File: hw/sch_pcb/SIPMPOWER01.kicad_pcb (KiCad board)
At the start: 2 copper layers, 60.5 x 40.1 mm, 37 parts, among them J1 HEADER_2x01_PARALLEL, J2 HEADER_2x01_PARALLEL, J3 HEADER_2x01_PARALLEL, J4 HEADER_2x01_PARALLEL, J5 HEADER_2x01_PARALLEL, J6 JUMP2_2x1, J7 HEADER_2x01, J8 HEADER_2x01, J9 HEADER_2x01, M1 HOLE, M2 HOLE, M3 HOLE, M4 HOLE

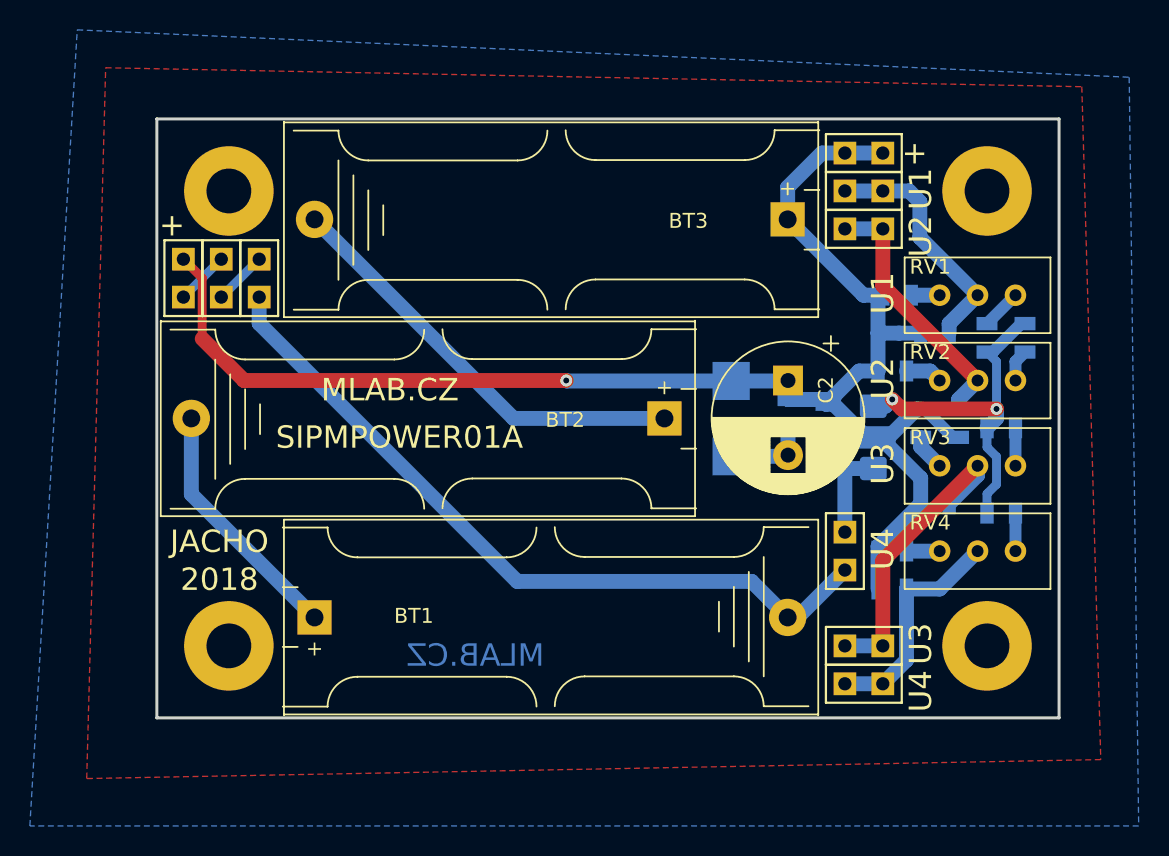
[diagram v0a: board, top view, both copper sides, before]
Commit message: Update to KiCADv7.
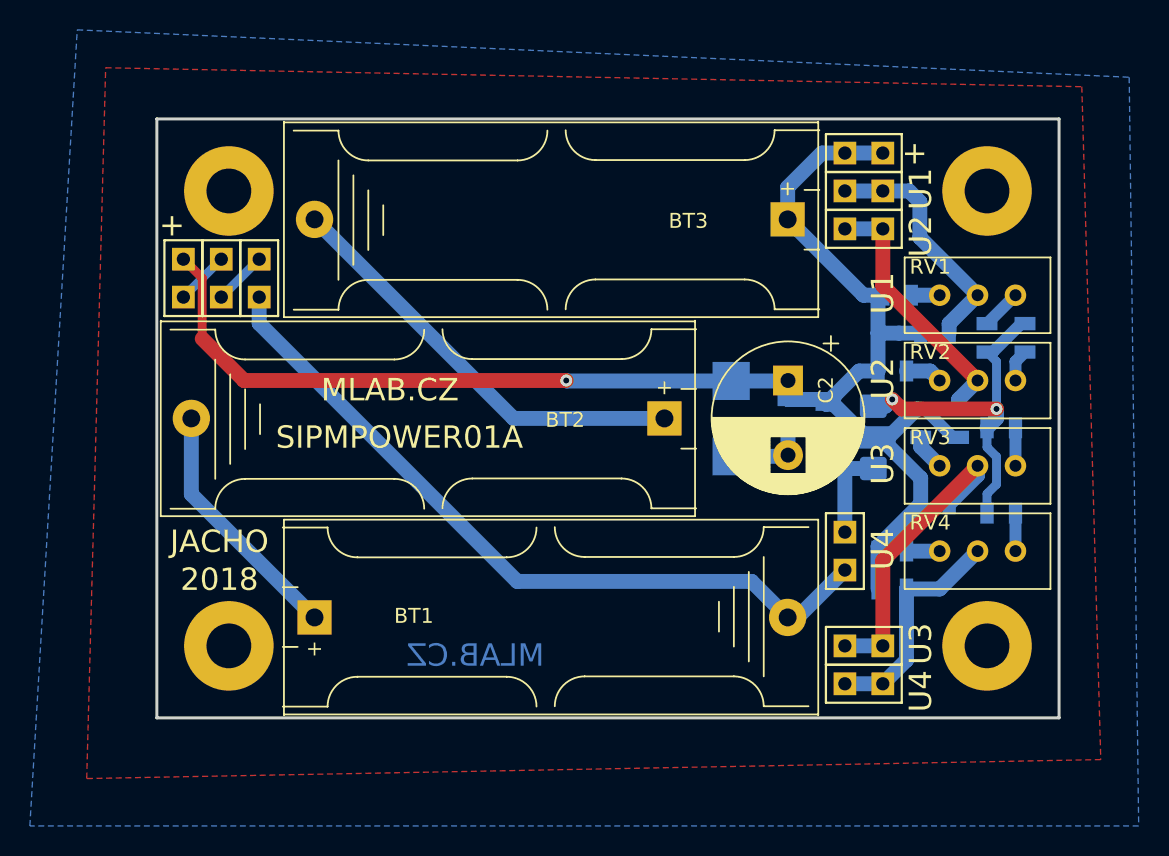
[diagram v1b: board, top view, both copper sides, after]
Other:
- net class Default removed
